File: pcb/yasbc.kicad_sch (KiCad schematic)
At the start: 188 parts, among them J1 BOOT, J10 Conn_02x20_Odd_Even, J2 USB TTY, J3 AudioJack3, J4 1V5, J5 3V3, J6 1V2, J7 USB DEV, J8 HDMI_A, J9 USB HOST, Q1 AO3401A, Q2 AO3401A, SW1 RESET, SW2 SW_SPDT, SW3 SW_SPDT, SW4 SW_SPDT, SW5 SW_SPDT, SW6 SW_5WAY, U1 BCT2028, U2 uSD_Card, U3 Allwinner_A13, U4 CH340E, U5 TD6810, U6 SE5120, U7 K4B4G1646E, U8 MPU-6050, U9 ADV7513, Y1 24M

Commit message: Schematic draft
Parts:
- removed C25: 1u, Capacitor_SMD:C_0603_1608Metric, symbol Device:C_Small
- removed C31, C39: 100n, Capacitor_SMD:C_0603_1608Metric, symbol Device:C_Small
- removed C32: DNF, Capacitor_SMD:C_0603_1608Metric, symbol Device:C_Small
- removed C44, C48: 10u, Capacitor_SMD:C_0603_1608Metric, symbol Device:C_Small
- removed J6: 1V2, Connector_PinHeader_2.54mm:PinHeader_1x02_P2.54mm_Vertical, symbol Connector_Generic:Conn_01x02
- removed R1, R12: 10K, Resistor_SMD:R_0603_1608Metric, symbol Device:R
- removed R30: 47K, Resistor_SMD:R_0603_1608Metric, symbol Device:R
- removed RN4: 47K, Resistor_SMD:R_Array_Convex_4x0603, symbol Device:R_Pack04_Split
- removed U1: BCT2028, Package_TO_SOT_SMD:SOT-23-5, symbol yasbc:BCT2028
- removed U5: TD6810, Package_TO_SOT_SMD:TSOT-23-5, symbol yasbc:TD6810
- removed U6: SE5120, Package_TO_SOT_SMD:SOT-223-3_TabPin2, symbol yasbc:SE5120
- added C10, C12: 6.8p, Capacitor_SMD:C_0603_1608Metric, symbol Device:C_Small
- added C11, C13: 33p, Capacitor_SMD:C_0603_1608Metric, symbol Device:C_Small
- added C18, C2, C26, C27, C3, C4, C6: 100n, Capacitor_SMD:C_0603_1608Metric, symbol Device:C_Small
- added C22, C23, C28: 10u, Capacitor_SMD:C_0603_1608Metric, symbol Device:C_Small
- added J7, J8: 1V5, Connector_PinHeader_2.54mm:PinHeader_1x02_P2.54mm_Vertical, symbol Connector_Generic:Conn_01x02
- added L2: 2.2u, Inductor_SMD:L_1008_2520Metric, symbol Device:L_Small
- added R10: 402K, symbol Device:R_Small
- added R11, R5: 200K, symbol Device:R_Small
- added R14, R15, R24, R25, R26: 47K, Resistor_SMD:R_0603_1608Metric, symbol Device:R
- added R4: 280K, symbol Device:R_Small
- added R6: 562K, symbol Device:R_Small
- added R7: 100K, symbol Device:R_Small
- added R8: 604K, symbol Device:R_Small
- added R9: 232K, symbol Device:R_Small
- added U1: LM26480, symbol yasbc:LM26480
- C1: value 1u -> 100n
- C5: value DNF -> 100n
- J5: value 3V3 -> 1V5
- L1: value 4.7u -> 2.2u
- renumbered C76 to C100, C91 to C101, C43 to C102, C77 to C103, C92 to C104, C51 to C105, C78 to C106, C93 to C107, C53 to C14, C83 to C15, C94 to C16, C95 to C17, C96 to C20, C97 to C21, C98 to C24, C99 to C25, C63 to C30, C64 to C31, C65 to C32, C62 to C33, C66 to C34, C67 to C35, C8 to C36, C9 to C37, C10 to C38, C11 to C39, C2 to C40, C12 to C41, C13 to C42, C3 to C43, C14 to C44, C15 to C45, C16 to C46, C4 to C47, C17 to C48, C21 to C49, C22 to C50, C7 to C51, C23 to C52, C60 to C53, C61 to C54, C58 to C55, C59 to C56, C35 to C57, C36 to C58, C33 to C59, C34 to C60, C52 to C61, C40 to C62, C37 to C63, C38 to C64, C41 to C65, C42 to C66, C46 to C67, C47 to C68, C57 to C69, C27 to C7, C56 to C70, C49 to C71, C50 to C72, C54 to C73, C55 to C74, C20 to C75, C18 to C76, C88 to C77, C24 to C78, C89 to C79, C6 to C8, C90 to C80, C82 to C81, C26 to C82, C70 to C83, C28 to C85, C72 to C86, C68 to C87, C79 to C88, C30 to C89, C45 to C9, C69 to C90, C80 to C91, C71 to C92, C81 to C93, C73 to C94, C85 to C95, C74 to C96, C86 to C97, C75 to C98, C87 to C99, D9 to D1, D1 to D2, D2 to D3, D3 to D4, D4 to D5, D5 to D6, D6 to D7, D7 to D8, D8 to D9, J2 to J1, J3 to J10, J10 to J11, J8 to J2, J7 to J3, J9 to J6, J1 to J9, R6 to R1, R16 to R12, R15 to R13, R20 to R16, R21 to R17, R22 to R18, R23 to R19, R5 to R2, R24 to R20, R25 to R21, R26 to R22, R27 to R23, R18 to R27, R19 to R28, R17 to R29, R40 to R3, R36 to R30, R37 to R31, R38 to R32, R39 to R33, R13 to R34, R14 to R35, R31 to R36, R32 to R37, R2 to R38, R28 to R39, R29 to R40, R7 to R41, R34 to R42, R35 to R43, R9 to R44, R8 to R45, R10 to R46, R11 to R47, R4 to R48, R3 to R49, R33 to R50, RN2 to RN1, RN3 to RN2, SW2 to SW1, SW3 to SW2, SW4 to SW3, SW5 to SW4, SW6 to SW5, SW1 to SW6, U9 to U2, U4 to U3, U3 to U4, U2 to U5, U8 to U6
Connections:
- net +1V2: now also J4.1 (Pin_1), L1.2, C10.1, C18.1, C22.1, R4.1
- net +1V5: now also C29.1, C27.1, J8.1 (Pin_1), R10.1, U1.23 (LDO2); no longer J4.1 (Pin_1)
- net +1V8: now also C26.1, C28.1, J7.1 (Pin_1), R8.1, U1.20 (LDO1)
- net +3V3: now also C19.1, C5.1, C12.1, C23.1, C6.1, L2.2, R6.1, U1.19 (VINLDO1), U1.24 (VINLDO2)
- net +5V: now also C1.2, C2.1, C3.1, C4.1, U1.1 (VINLDO12), U1.10 (AVDD), U1.12 (ENSW2), U1.13 (VIN2), U1.16 (ENLDO2), U1.17 (ENLDO1), U1.6 (VIN1), U1.7 (ENSW1); no longer C1.1, C29.1
- net GND: now also C1.1, J4.2 (Pin_2), J5.2 (Pin_2), C11.2, C13.2, C18.2, C2.2, C22.2, C23.2, C26.2, C27.2, C28.2, C3.2, C4.2, C6.2, J7.2 (Pin_2), J8.2 (Pin_2), R11.2, R14.2, R15.2, R24.2, R25.2, R26.2, R5.2, R7.2, R9.2, U1.15 (GND_SW2), U1.18 (GND_L), U1.2 (SYNC), U1.4 (GND_SW1), U1.9 (GND_C), U1.DAP; no longer C1.2
- net SW_CENTER: now also R25.1
- net SW_DOWN: now also R14.1
- net SW_LEFT: now also R26.1
- net SW_RIGHT: now also R24.1
- net SW_UP: now also R15.1
- net P_SW1: now reaches L1.1
- net P_SW1: now also U1.5 (SW1)
- new net P_FB1: C10.2, C11.1, R4.2, R5.1, U1.8 (FB1)
- new net P_FB2: C12.2, C13.1, R6.2, R7.1, U1.11 (FB2)
- new net P_FBL1: R8.2, R9.1, U1.21 (FBL1)
- new net P_FBL2: R10.2, R11.1, U1.22 (FBL2)
- new net P_SW2: L2.1, U1.14 (SW2)
- no-connect marks 44 -> 45
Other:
- note added: "0.5 * (280 + 200)/200"
- note added: "0.5 * (402 + 200)/200"
- note added: "0.5 * (562 + 100)/100"
- note added: "0.5 * (604 + 232)/232"
- note added: "1V2 Rail (Core)"
- note added: "1V5 Rail (DRAM)"
- note added: "1V8 Rail (HDMI)"
- note added: "3V3 Rail (IO)"
- note added: "POWER SUPPLY (3V3, 1V8, 1V5, 1V2)"
- note removed: "CORE POWER"
- note removed: "DRAM POWER"
- note removed: "IO POWER"
- note removed: "POWER SUPPLY (1V2)"
- note removed: "POWER SUPPLY (1V5)"
- note removed: "POWER SUPPLY (3V3)"
- moved on the sheet: C30, C31, C32, C34, C35, D1, SW5

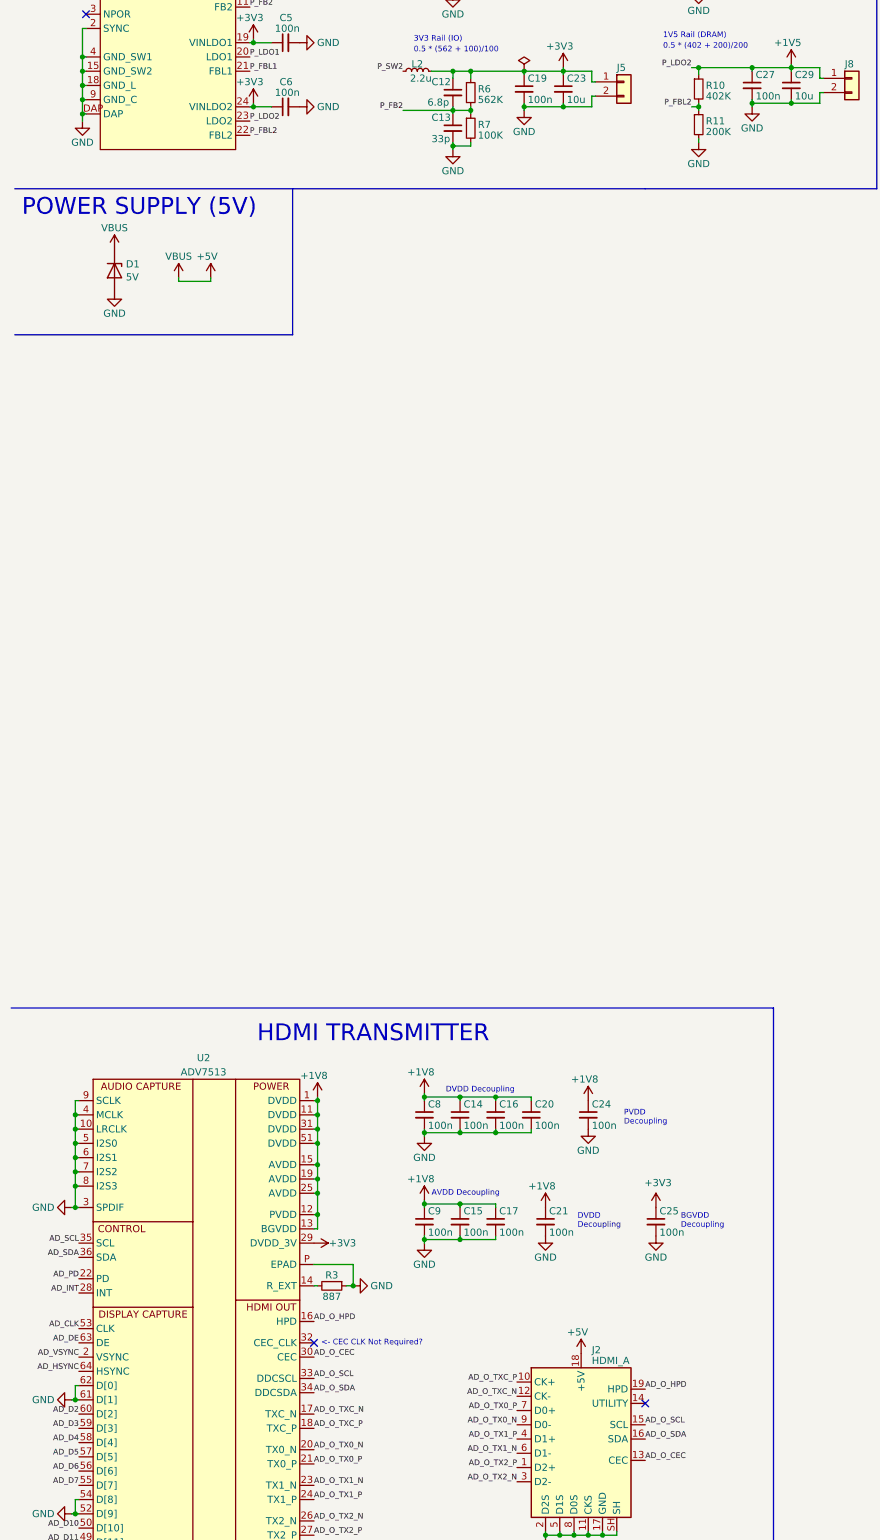
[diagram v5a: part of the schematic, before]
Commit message: PMIC PCB layout
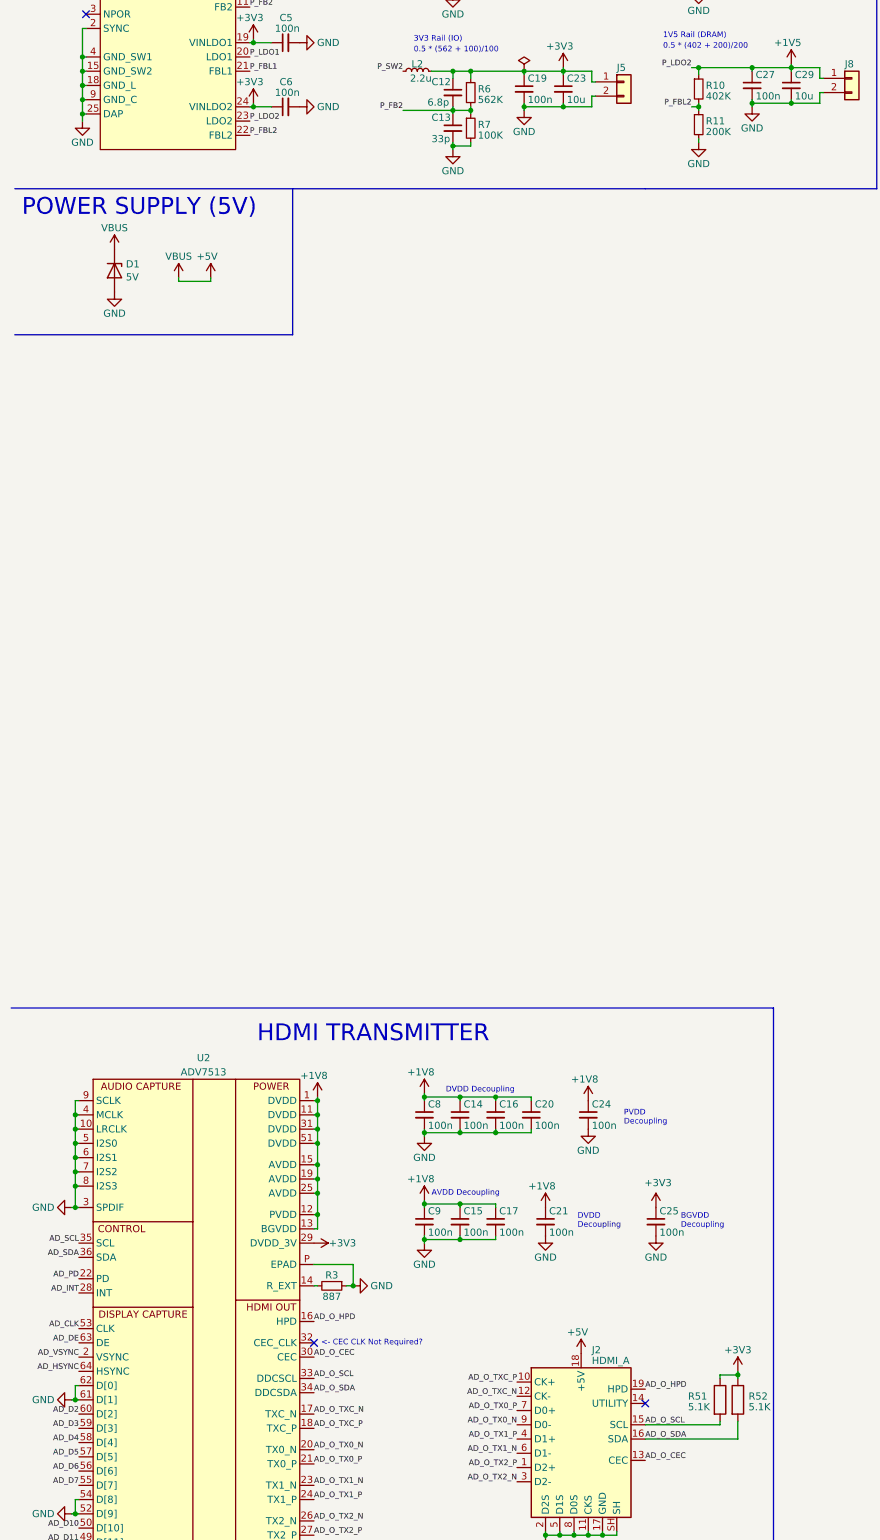
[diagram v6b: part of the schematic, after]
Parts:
- added R51, R52: 5.1K, Resistor_SMD:R_0603_1608Metric, symbol Device:R
- C56, C87: footprint (none) -> Capacitor_SMD:C_0603_1608Metric
- F1: footprint Fuse:Fuse_0805_2012Metric_Castellated -> Fuse:Fuse_0805_2012Metric_Pad1.15x1.40mm_HandSolder
- L1, L2: footprint Inductor_SMD:L_1008_2520Metric -> yasbc:Inductor_5.2x5.8x4.5mm
- R10, R11, R4, R5, R6, R7, R8, R9: footprint (none) -> Resistor_SMD:R_0603_1608Metric
- U1: footprint (none) -> Package_DFN_QFN:WQFN-24-1EP_4x4mm_P0.5mm_EP2.6x2.6mm
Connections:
- net +3V3: now also R51.1, R52.1
- net AD_O_SCL: now also R51.2
- net AD_O_SDA: now also R52.2
- net GND: now also U1.25 (DAP); no longer U1.DAP

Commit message: PCB progress
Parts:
- added R53, R54: 5.1K, Resistor_SMD:R_0603_1608Metric, symbol Device:R
- C1, C10, C100, C101, C103, C104, C106, C107, C11, C12, C13, C14, C15, C16, C17, C18, C19, C2, C20, C21, C22, C23, C24, C25, C26, C27, C28, C29, C3, C30, C31, C32, C33, C34, C35, C36, C37, C38, C39, C4, C41, C42, C43, C44, C45, C46, C47, C48, C49, C5, C50, C51, C52, C53, C54, C55, C57, C58, C59, C6, C60, C61, C62, C63, C64, C65, C66, C67, C68, C69, C7, C70, C71, C72, C75, C76, C77, C78, C79, C8, C80, C81, C82, C83, C84, C85, C86, C88, C89, C9, C90, C91, C92, C93, C94, C95, C96, C97, C98, C99: footprint Capacitor_SMD:C_0603_1608Metric -> Capacitor_SMD:C_0402_1005Metric
- C56: value 47u -> 10u; footprint Capacitor_SMD:C_0603_1608Metric -> Capacitor_SMD:C_0402_1005Metric
- D2, D3, D4, D5, D6, D7, D8, D9: footprint LED_SMD:LED_1206_3216Metric -> LED_SMD:LED_0603_1608Metric
- J2: footprint (none) -> Connector_HDMI:HDMI_A_Molex_208658-1001_Horizontal
- R10: value 402K -> 604K
- R11: value 200K -> 232K
- R8: value 604K -> 402K
- R9: value 232K -> 200K
- U2: footprint (none) -> Package_QFP:LQFP-64-1EP_10x10mm_P0.5mm_EP5x5mm
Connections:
- net +1V5: now also C26.1, C28.1, J7.1 (Pin_1), R8.1, U1.20 (LDO1); no longer C27.1, C29.1, J8.1 (Pin_1), R10.1, U1.23 (LDO2)
- net +1V8: now also C27.1, C29.1, J8.1 (Pin_1), R10.1, U1.23 (LDO2); no longer C26.1, C28.1, J7.1 (Pin_1), R8.1, U1.20 (LDO1)
- net +3V3: now also R53.1, R54.1
- net AD_SCL: now also R53.2
- net AD_SDA: now also R54.2
- net GND: now also U2.65 (EPAD); no longer U2.P (EPAD)
- net LED1: now also RN1.1 (R1.1); no longer RN1.2 (R2.1)
- net LED2: now also RN1.2 (R2.1); no longer RN1.3 (R3.1)
- net LED3: now also RN1.3 (R3.1); no longer RN1.1 (R1.1)
- net LED5: now also RN2.1 (R1.1); no longer RN2.5 (R4.2)
- net LED6: now also RN2.2 (R2.1); no longer RN2.8 (R1.2)
- net LED7: now also RN2.3 (R3.1); no longer RN2.6 (R3.2)
- net LED8: now also RN2.4 (R4.1); no longer RN2.7 (R2.2)
- net TTY_RX: now also TP1.1; no longer TP2.1
- net TTY_TX: now also TP2.1; no longer TP1.1
- net at D9.2 (A): now also RN2.5 (R4.2); no longer RN2.4 (R4.1)
- net at D6.2 (A): now also RN2.8 (R1.2); no longer RN2.1 (R1.1)
- net at D8.2 (A): now also RN2.6 (R3.2); no longer RN2.3 (R3.1)
- net at D7.2 (A): now also RN2.7 (R2.2); no longer RN2.2 (R2.1)
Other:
- moved on the sheet: C85, C89, RN2, TP1, TP2, TP3
